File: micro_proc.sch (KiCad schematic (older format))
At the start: 2 parts, among them U30 MSP430G2203IPW28

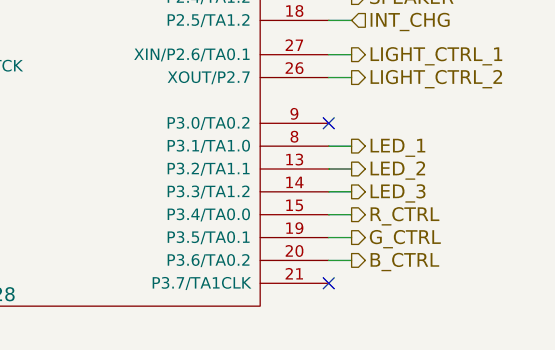
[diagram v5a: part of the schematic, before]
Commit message: finished routing board, added vibrator module
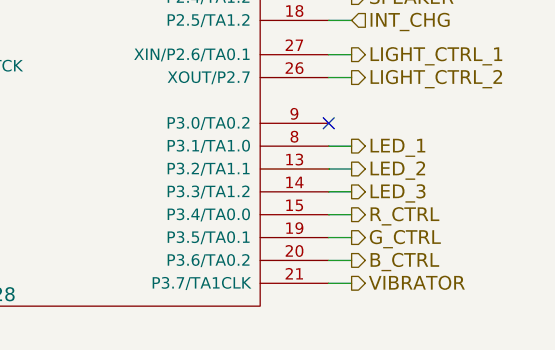
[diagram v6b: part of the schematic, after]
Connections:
- net VIBRATOR: now reaches U30.21 (P3.7/TA1CLK)
- no-connect marks 4 -> 3
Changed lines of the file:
@@
 Sheet 4 16
 Title ""
-Date "16 feb 2014"
+Date "17 feb 2014"
 Rev ""
 Comp ""
@@
 NoConn ~ 4200 2750
 NoConn ~ 7800 2900
-NoConn ~ 7800 3600
+Text HLabel 7900 3600 2    60   Output ~ 0
+VIBRATOR
+Wire Wire Line
+	7800 3600 7900 3600
 $EndSCHEMATC
